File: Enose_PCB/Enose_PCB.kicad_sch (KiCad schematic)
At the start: 56 parts, among them IC3 TPS22958DGNR, J1 Conn_01x04_Pin, J10 Fan, J11 Conn_01x04_Pin, J12 DA15_Pins_MountingHoles, J2 Conn_01x04_Pin, J3 Conn_01x04_Pin, Q6 NMOS, SW1 SW_SPST, SW2 SW_SPST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

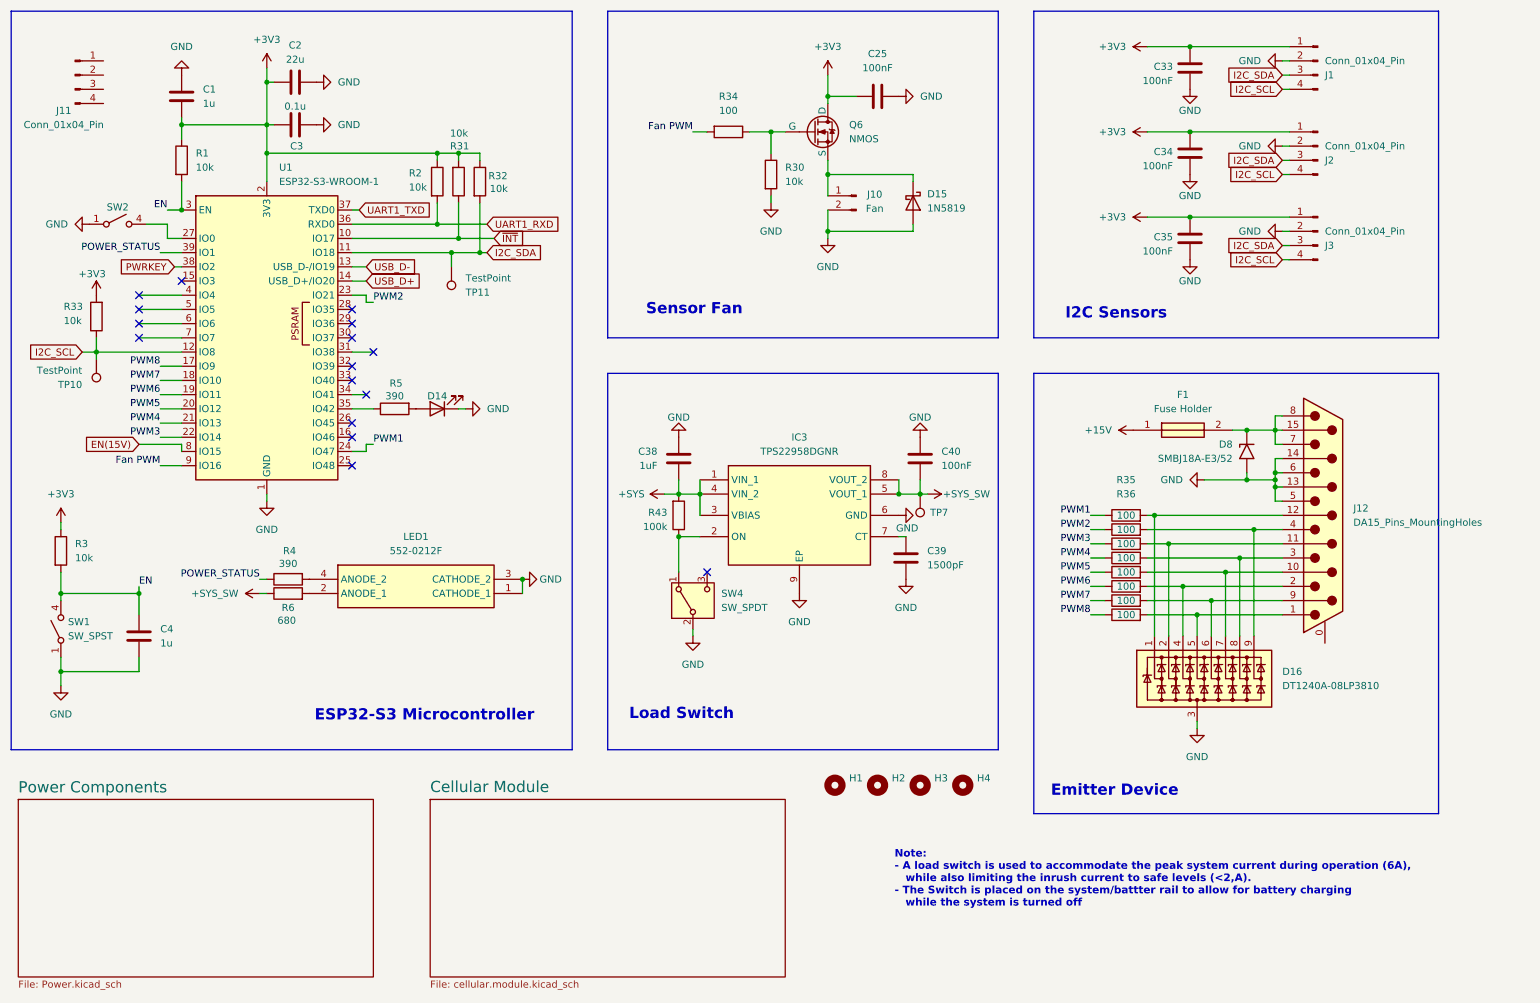
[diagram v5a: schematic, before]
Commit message: Enose board ready for review
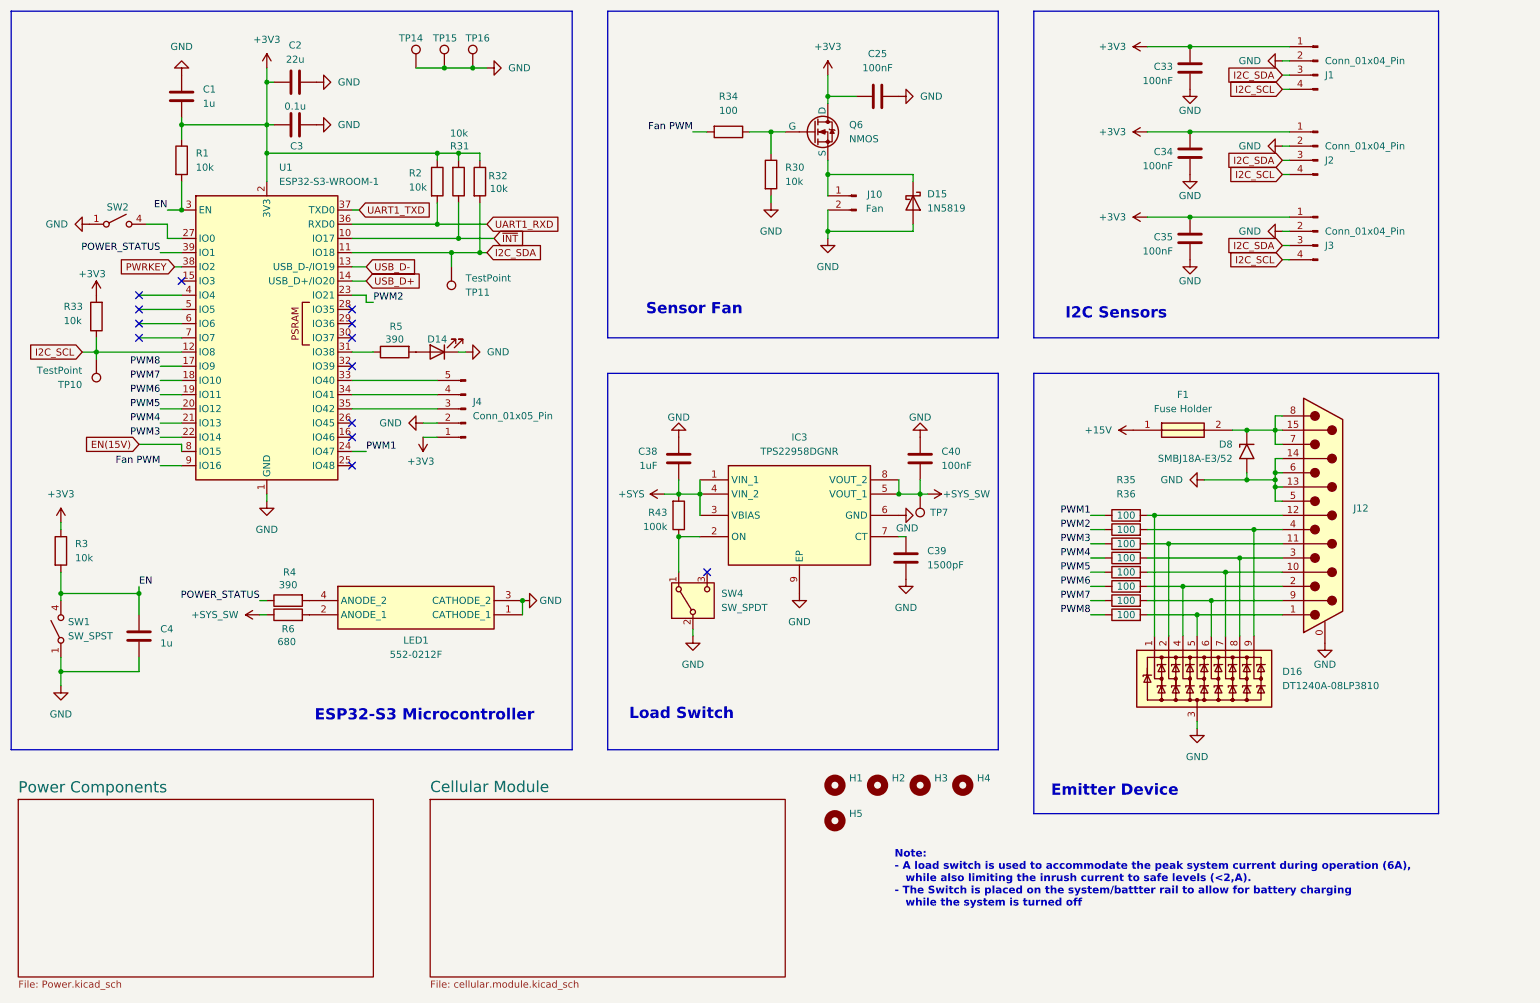
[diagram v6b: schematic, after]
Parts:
- removed J11: Conn_01x04_Pin, symbol Connector:Conn_01x04_Pin
- added H5: MountingHole, MountingHole:MountingHole_3.2mm_M3, symbol Mechanical:MountingHole
- added J4: Conn_01x05_Pin, Connector_PinHeader_2.54mm:PinHeader_1x05_P2.54mm_Vertical, symbol Connector:Conn_01x05_Pin
- added TP14, TP15, TP16: TestPoint, TestPoint:TestPoint_Pad_D1.5mm, symbol Connector:TestPoint
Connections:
- net +3V3: now also J4.1 (Pin_1)
- net GND: now also J12.0 (PAD), J4.2 (Pin_2), TP14.1, TP15.1, TP16.1
- net at R5.1: now also U1.31 (IO38); no longer U1.35 (IO42)
- net at U1.33 (IO40): now also J4.5 (Pin_5)
- net at U1.34 (IO41): now also J4.4 (Pin_4)
- new net: J4.3 (Pin_3), U1.35 (IO42)
- no-connect marks 16 -> 13
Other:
- moved on the sheet: D14, LED1, R4, R5, R6
